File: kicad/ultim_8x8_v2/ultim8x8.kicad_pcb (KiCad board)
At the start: 2 copper layers, 61 x 61 mm, 92 parts, among them P1 Input1, P10 DO_H, P11 5V, P12 GND, P13 CI_A, P14 CO_H, P15 DI_A, P16 DO_H, P17 5V, P18 5V, P19 GND, P2 Output1, P20 GND, P3 5V, P4 GND, P5 Input2, P6 Output2, P7 CI_A, P8 CO_H, P9 DI_A, U01 APA102, U02 APA102, U03 APA102, U04 APA102, U05 APA102, U06 APA102, U07 APA102, U08 APA102, U09 APA102, U10 APA102, U11 APA102, U12 APA102, U13 APA102, U14 APA102, U15 APA102, U16 APA102, U17 APA102, U18 APA102, U19 APA102, U20 APA102, U21 APA102, U22 APA102, U23 APA102, U24 APA102, U25 APA102, U26 APA102, U27 APA102, U28 APA102, U29 APA102, U30 APA102, U31 APA102, U32 APA102, U33 APA102, U34 APA102, U35 APA102, U36 APA102, U37 APA102, U38 APA102, U39 APA102, U40 APA102, U41 APA102, U42 APA102, U43 APA102, U44 APA102, U45 APA102, U46 APA102, U47 APA102, U48 APA102, U49 APA102, U50 APA102, U51 APA102, U52 APA102, U53 APA102, U54 APA102, U55 APA102, U56 APA102, U57 APA102, U58 APA102, U59 APA102, U60 APA102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

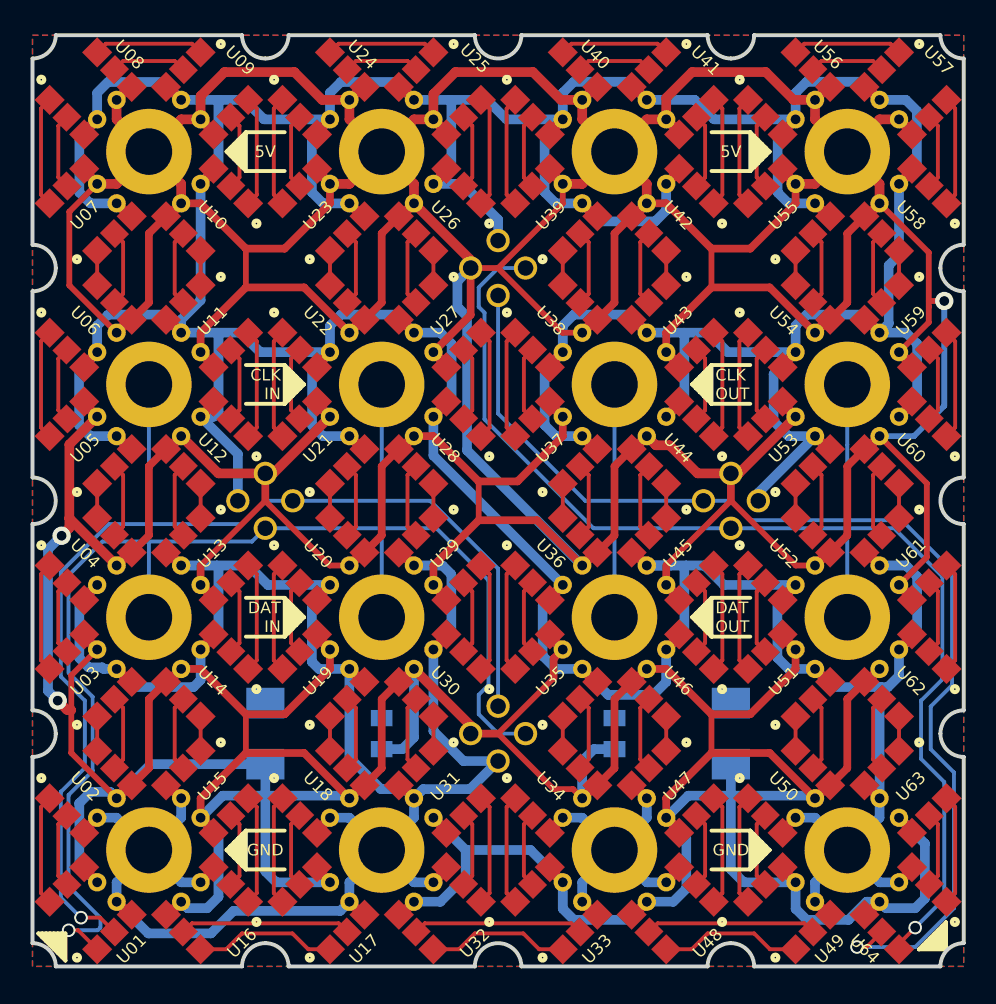
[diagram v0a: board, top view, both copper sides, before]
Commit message: U88 ver2 with extra power / signal mounting holes
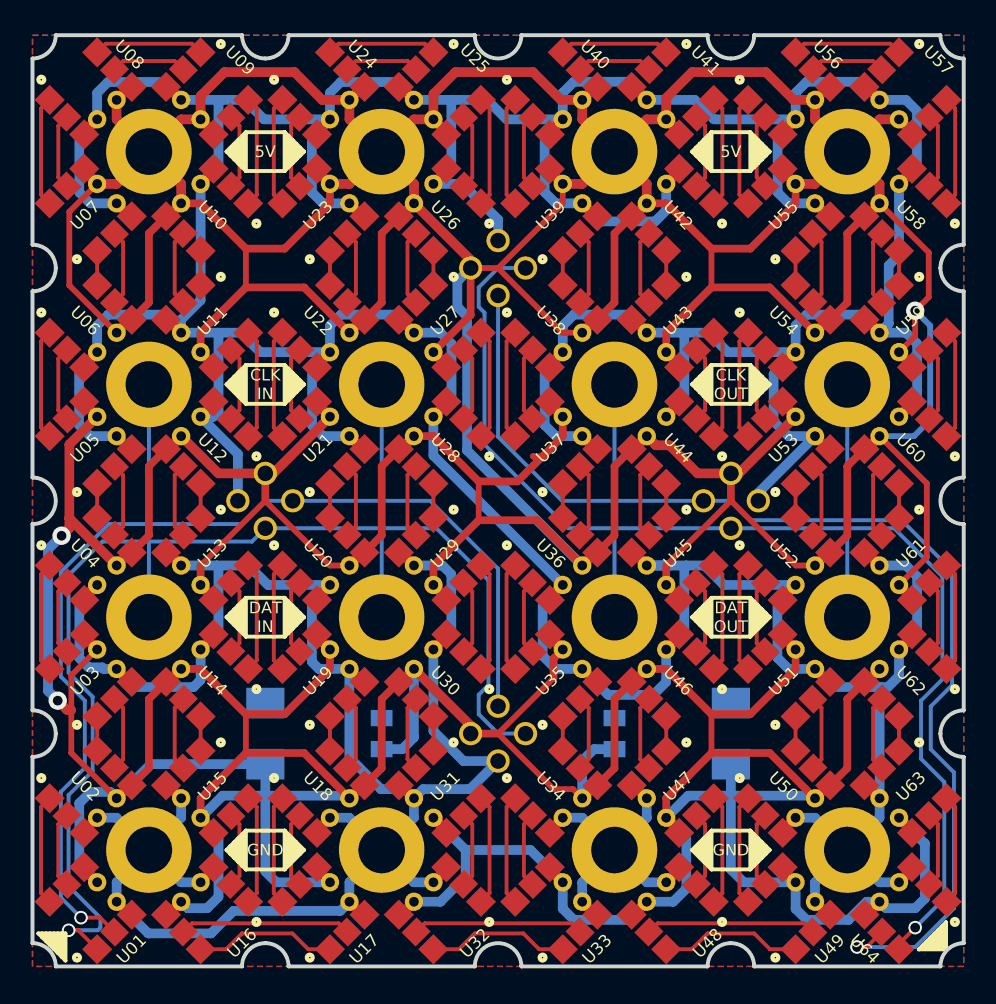
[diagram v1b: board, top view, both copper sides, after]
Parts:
- L1: footprint ultim8x8_libs:logo_ultim8x8 -> ultim8x8_libs:logo_ultim8x8_7mm
- L3: footprint ultim8x8_libs:logo_wyo_butterfly -> ultim8x8_libs:logo_wyo_butterfly_5mm
- L4: footprint ultim8x8_libs:logo_MLlabs -> ultim8x8_libs:logo_MLlabs_5mm
- P1: value Input1 -> In1
- P10: value DO_H -> D_OUT
- P2: value Output1 -> Out1
- P5: value Input2 -> In2
- P6: value Output2 -> Out2
- P7: value CI_A -> C_IN
- P8: value CO_H -> C_OUT
- P9: value DI_A -> D_IN
- moved L2 48.6 mm to (59.7, 82.5)
- moved L4 30.2 mm to (44.5, 43.2)
- moved L3 1.63 mm to (74.9, 43.2)
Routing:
- net /DO_H: track 85.1 -> 86.1 mm
- net /CO_H: track 91.0 -> 91.8 mm
- net /5V: track 786.9 -> 786.1 mm
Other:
- board text added: "+5V C_IN"
- board text added: "+5V C_OUT"
- board text added: "C_IN D_IN"
- board text added: "C_OUT D_OUT"
- board text added: "GND D_IN"
- board text added: "GND D_OUT"
- board text added: "maniacallabs.com"
- board text added: "wyolum.com"
- board text removed: "+5V CI_A"
- board text removed: "+5V CO_H"
- board text removed: "CI_A DI_A"
- board text removed: "CO_H DO_H"
- board text removed: "GND DI_A"
- board text removed: "GND DO_H"
- board text removed: "wyolum.com maniacallabs.com"
